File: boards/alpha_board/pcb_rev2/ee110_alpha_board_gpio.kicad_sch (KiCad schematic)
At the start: 37 parts, among them J3 keypad, J4 Micro_SD_Card, J5 SERVO1, J6 SERVO2, U10 MPU-9250, U6 74LS138, U7 74LVC245, U8 LM386, U9 LM2902

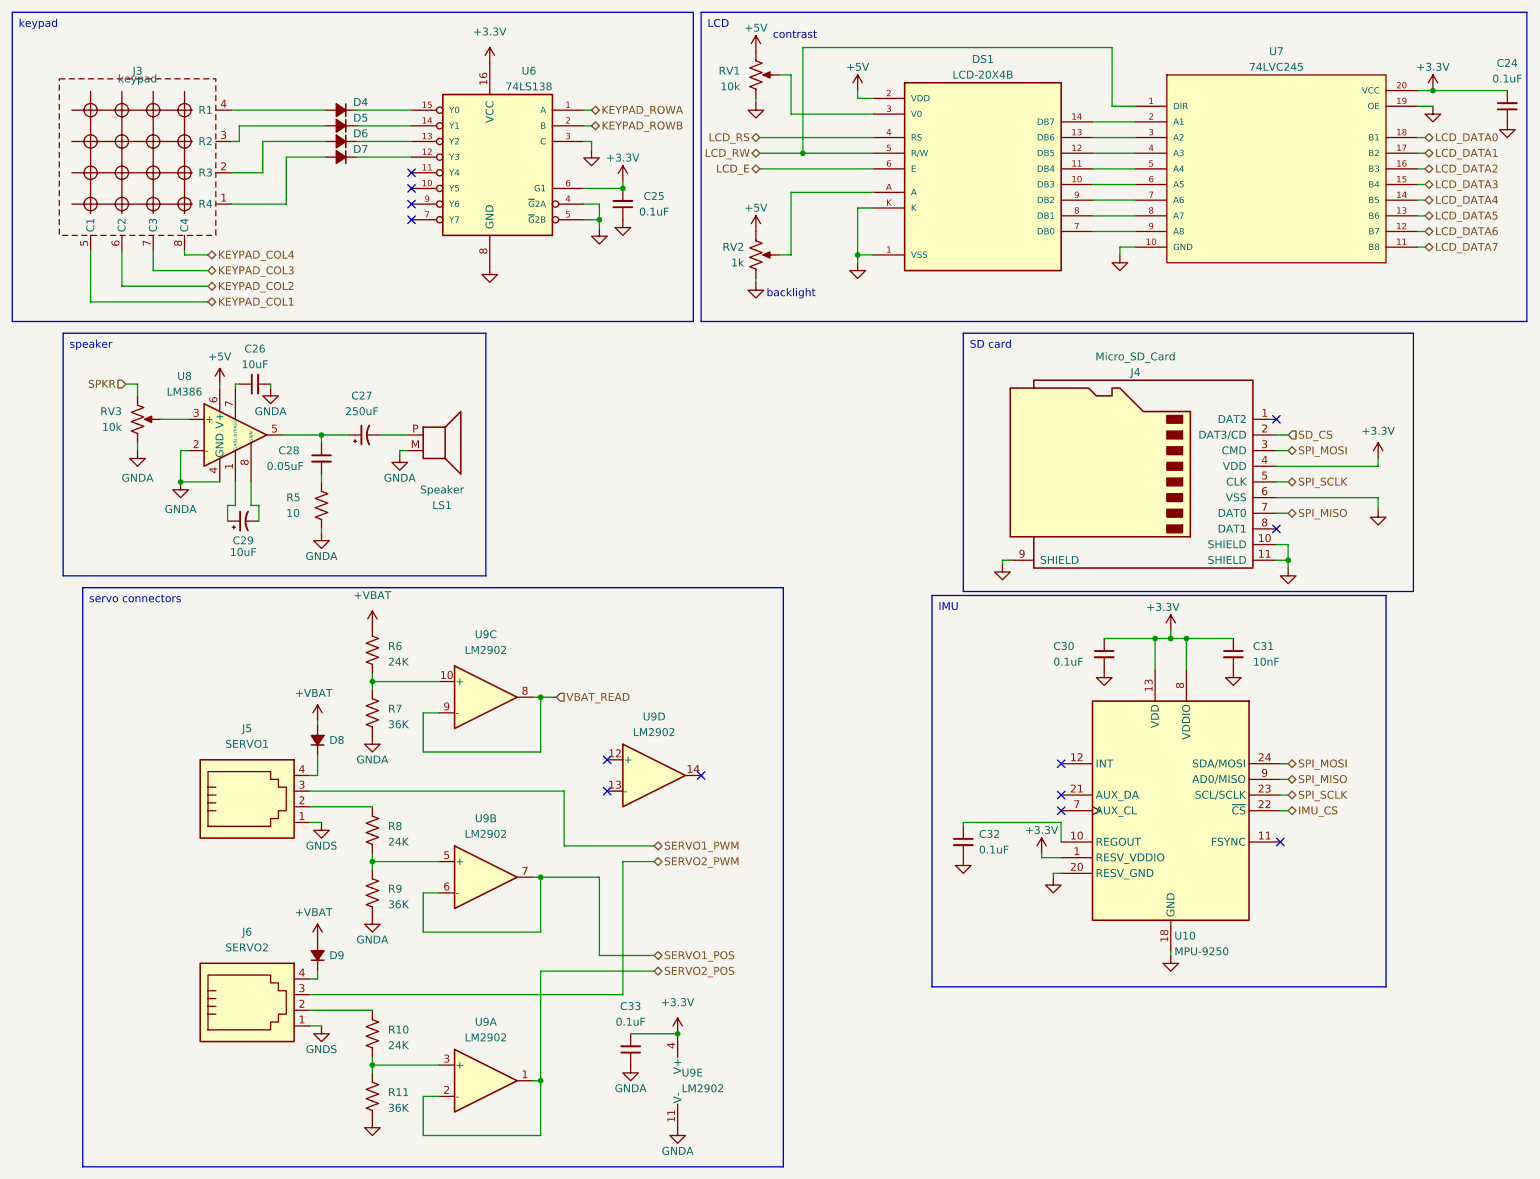
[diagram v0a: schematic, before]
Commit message: split body-back, body-top and body-front into smaller parts
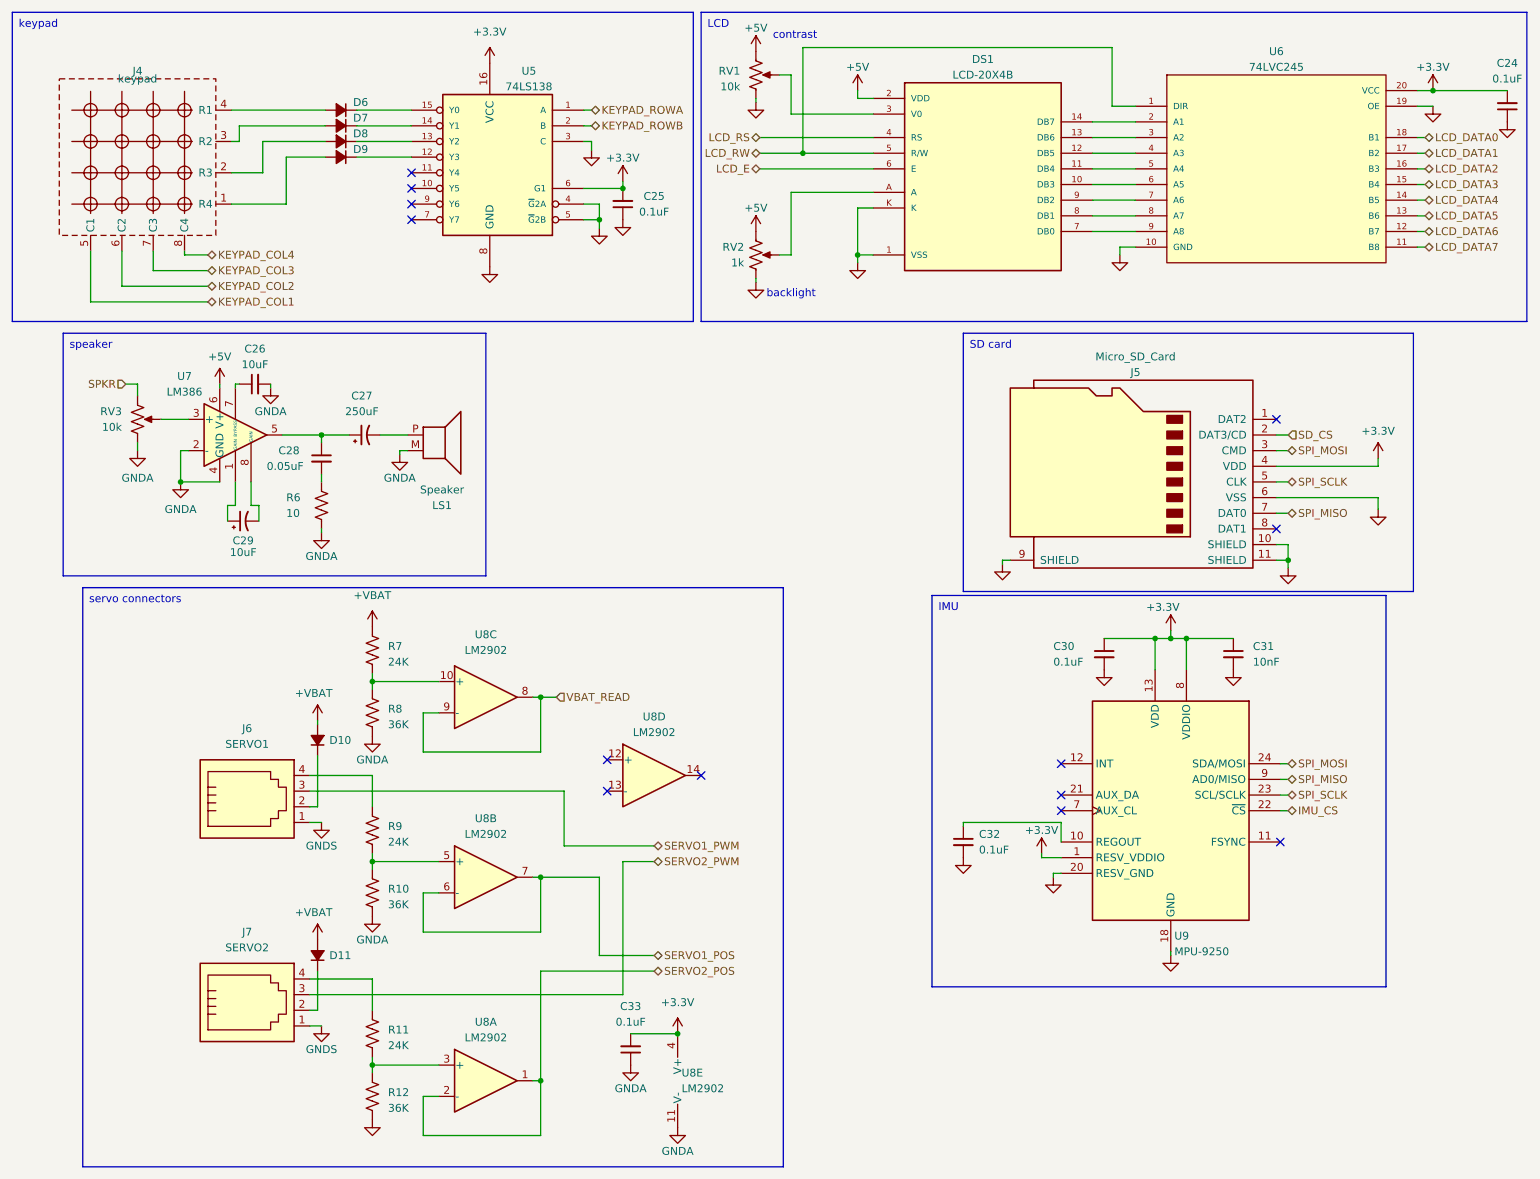
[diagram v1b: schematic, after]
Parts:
- D10: renamed from D8; footprint Diode_SMD:D_SOD-323F -> Diode_THT:D_DO-15_P12.70mm_Horizontal
- D11: renamed from D9; footprint Diode_SMD:D_SOD-323F -> Diode_THT:D_DO-15_P12.70mm_Horizontal
- LS1: footprint Alpha Board rev2 library:CUI_CVS-3108 -> Alpha Board rev2 library:SPKR_CVS-1508
- U6: renamed from U7; footprint Package_SO:SOIC-16_3.9x9.9mm_P1.27mm -> Package_SO:SOIC-20W_7.5x15.4mm_P1.27mm
- renumbered D4 to D6, D5 to D7, D6 to D8, D7 to D9, J3 to J4, J4 to J5, J5 to J6, J6 to J7, R9 to R10, R10 to R11, R11 to R12, R5 to R6, R6 to R7, R7 to R8, R8 to R9, U6 to U5, U8 to U7, U9 to U8, U10 to U9
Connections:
- net at J7.2: now also D11.1 (K); no longer R11.1
- net at J7.4: now also R11.1; no longer D11.1 (K)
- net at D10.1 (K): now also J6.2; no longer J6.4
- net at R9.1: now also J6.4; no longer J6.2

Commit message: 4/27
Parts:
- added D3: TEST_GREEN, LED_SMD:LED_0805_2012Metric_Pad1.15x1.40mm_HandSolder, symbol Device:LED
- added D4: TEST_BLUE, LED_SMD:LED_0805_2012Metric_Pad1.15x1.40mm_HandSolder, symbol Device:LED
- added D5: POWER_LED, LED_THT:LED_D3.0mm, symbol Device:LED
- added R2: 100, Resistor_SMD:R_0805_2012Metric_Pad1.20x1.40mm_HandSolder, symbol Device:R_US
- added R3, R4: 200, Resistor_SMD:R_0805_2012Metric_Pad1.20x1.40mm_HandSolder, symbol Device:R_US
- added R5: 280, Resistor_SMD:R_0805_2012Metric_Pad1.20x1.40mm_HandSolder, symbol Device:R_US
- added SW2: TEST_BUTTON, Button_Switch_SMD:SW_SPST_TL3342, symbol Switch:SW_Push
- added TP1: DIO22, TestPoint:TestPoint_THTPad_2.0x2.0mm_Drill1.0mm, symbol Connector:TestPoint
- added TP2: DIO23, TestPoint:TestPoint_THTPad_2.0x2.0mm_Drill1.0mm, symbol Connector:TestPoint
- added TP3: DIO24, TestPoint:TestPoint_THTPad_2.0x2.0mm_Drill1.0mm, symbol Connector:TestPoint
- added TP4: +3.3V, TestPoint:TestPoint_THTPad_2.0x2.0mm_Drill1.0mm, symbol Connector:TestPoint
- added TP5: GND, TestPoint:TestPoint_THTPad_2.0x2.0mm_Drill1.0mm, symbol Connector:TestPoint
- U9: footprint Package_DFN_QFN:QFN-24-1EP_3x3mm_P0.4mm_EP1.75x1.6mm -> Alpha Board rev2 library:QFN-24-1EP_3x3mm_P0.4mm_EP1.75x1.6mm
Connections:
- net +3.3V: now also U7.6 (V+), TP4.1
- net +5V: now also R5.1; no longer U7.6 (V+)
- net GND: now also D3.1 (K), D4.1 (K), D5.1 (K), SW2.1, TP5.1
- net GNDA: now also RV3.1; no longer RV3.3
- net SPKR: now also RV3.3; no longer RV3.1
- new net: R2.1, SW2.2
- new net: D3.2 (A), R3.1
- new net: D5.2 (A), R5.2
- new net: D4.2 (A), R4.1
- new net TEST_BLUE: R4.2, TP3.1
- new net TEST_BUTTON: R2.2, TP1.1
- new net TEST_GREEN: R3.2, TP2.1
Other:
- moved on the sheet: C26, C27, C28, C29, C30, C31, C32, C33, D10, D11, J5, J6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
